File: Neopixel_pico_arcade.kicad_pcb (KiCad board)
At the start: 4 copper layers, 100 x 100 mm, 147 parts, among them J1 SWD_connector, J2 NES_controller_connector, J3 USB_C_Receptacle_USB2.0, Q1 2N7002, U1 RP2040_Stamp, U2 SN74LV1T34DBV, U3 SRV05-4HTG-D

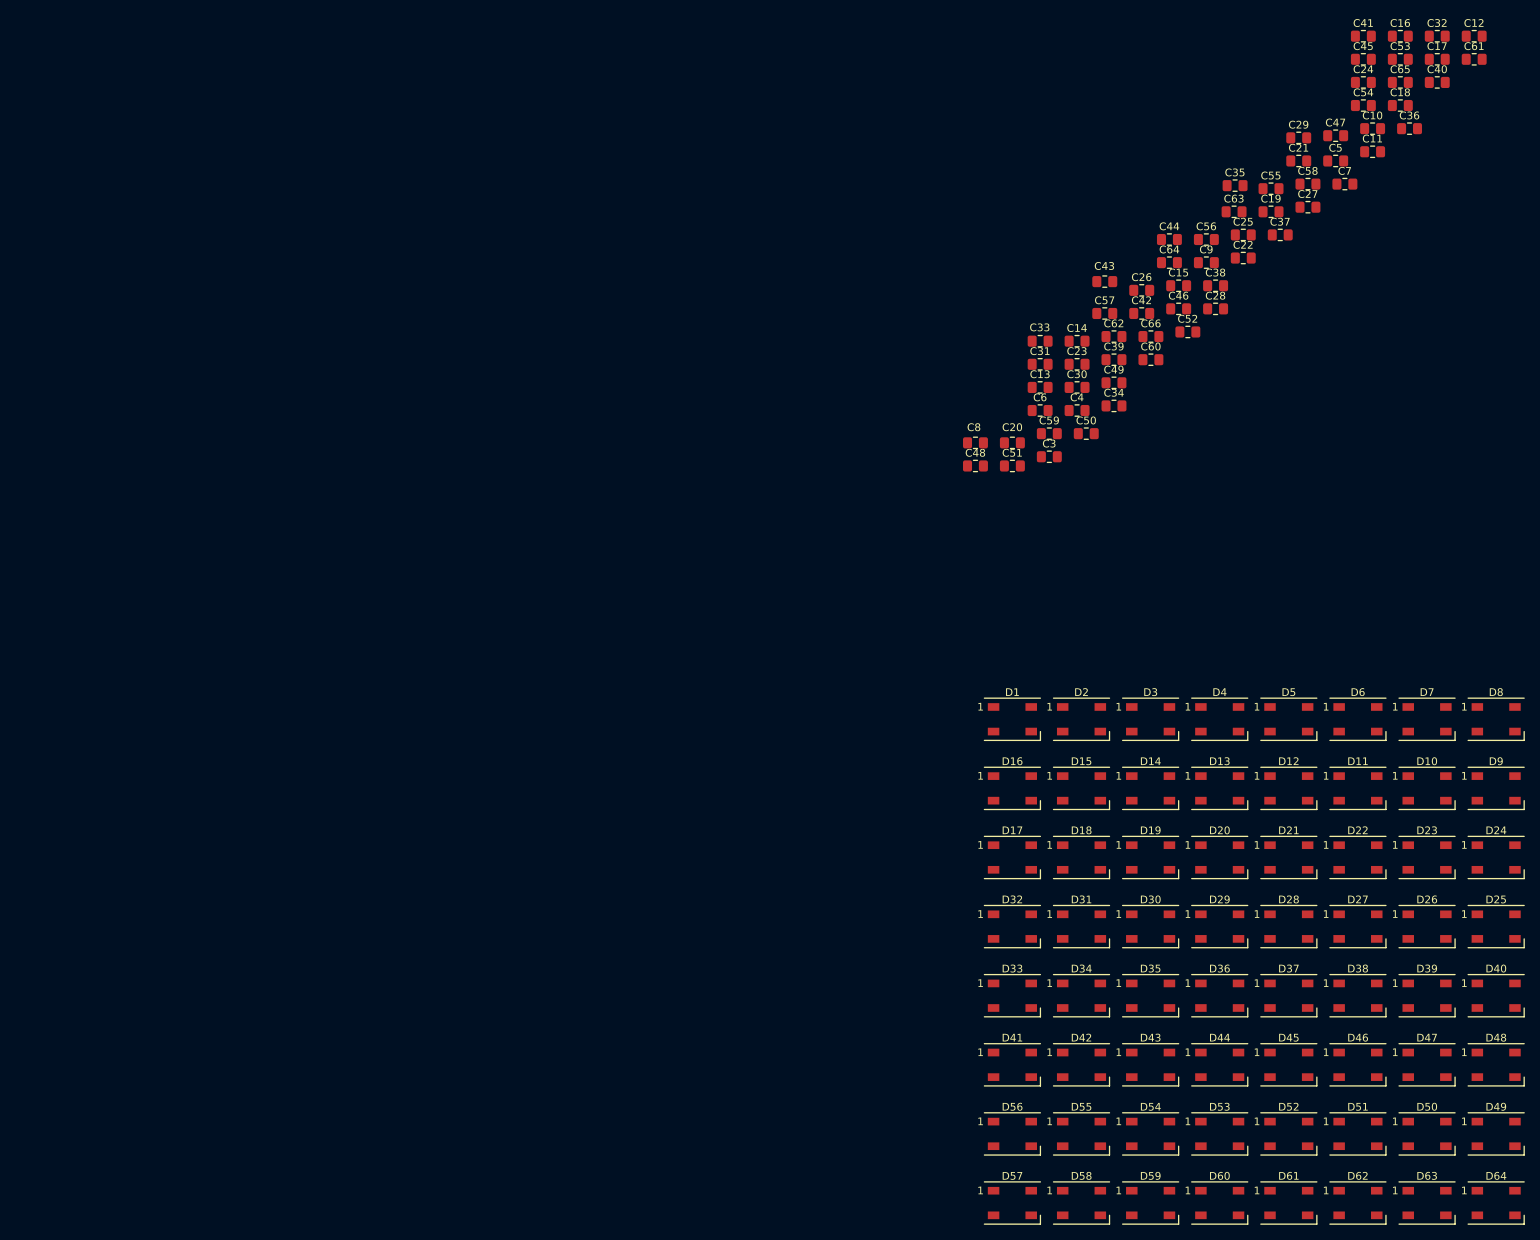
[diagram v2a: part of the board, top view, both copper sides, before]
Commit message: Arranges capacitors in the LED matrix
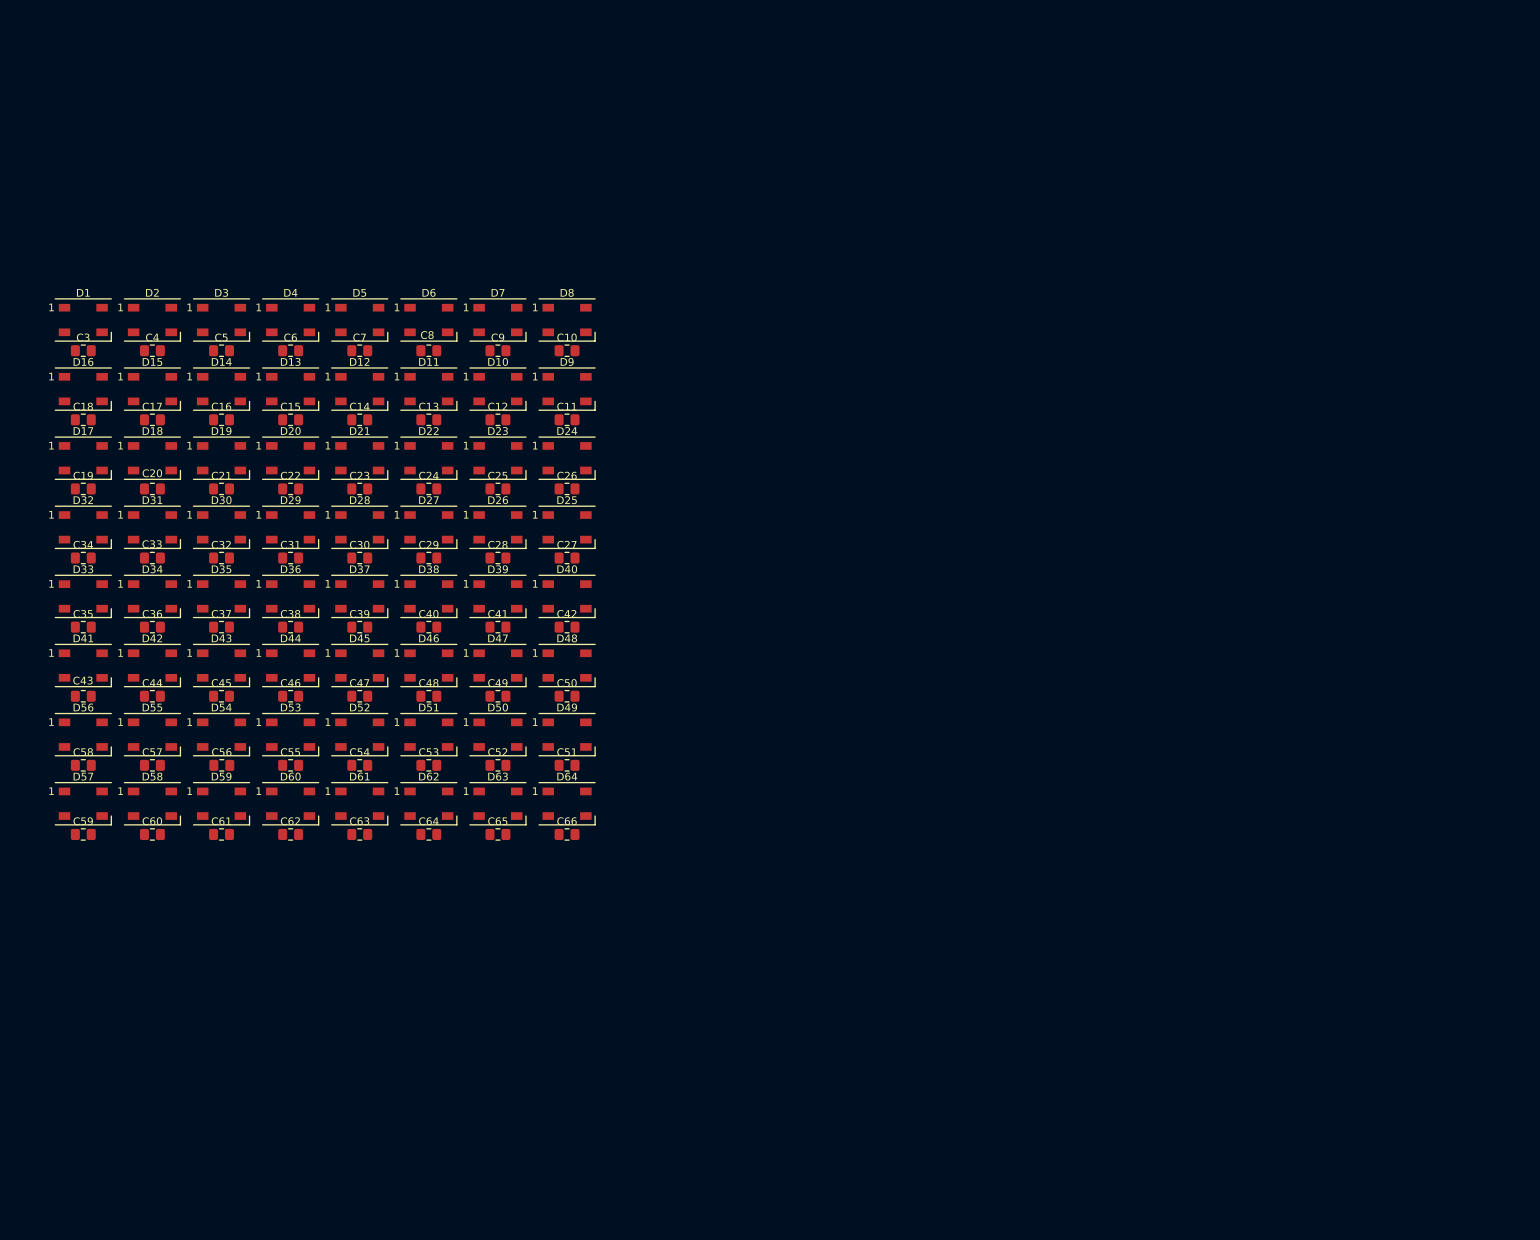
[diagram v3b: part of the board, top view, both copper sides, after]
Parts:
- moved C61 191.8 mm to (240.0, 135.0)
- moved C58 176.5 mm to (222.0, 126.0)
- moved C18 176.3 mm to (222.0, 81.0)
- moved C36 176.1 mm to (231.0, 108.0)
- moved C17 173.8 mm to (231.0, 81.0)
- moved C32 172.3 mm to (240.0, 99.0)
- moved C45 170.3 mm to (240.0, 117.0)
- moved C16 161.4 mm to (240.0, 81.0)
- moved C35 160.6 mm to (222.0, 108.0)
- moved C19 158.8 mm to (222.0, 90.0)
- moved C54 156.4 mm to (258.0, 126.0)
- moved C53 156.4 mm to (267.0, 126.0)
- moved C65 153.0 mm to (276.0, 135.0)
- moved C40 149.3 mm to (267.0, 108.0)
- moved C55 148.1 mm to (249.0, 126.0)
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
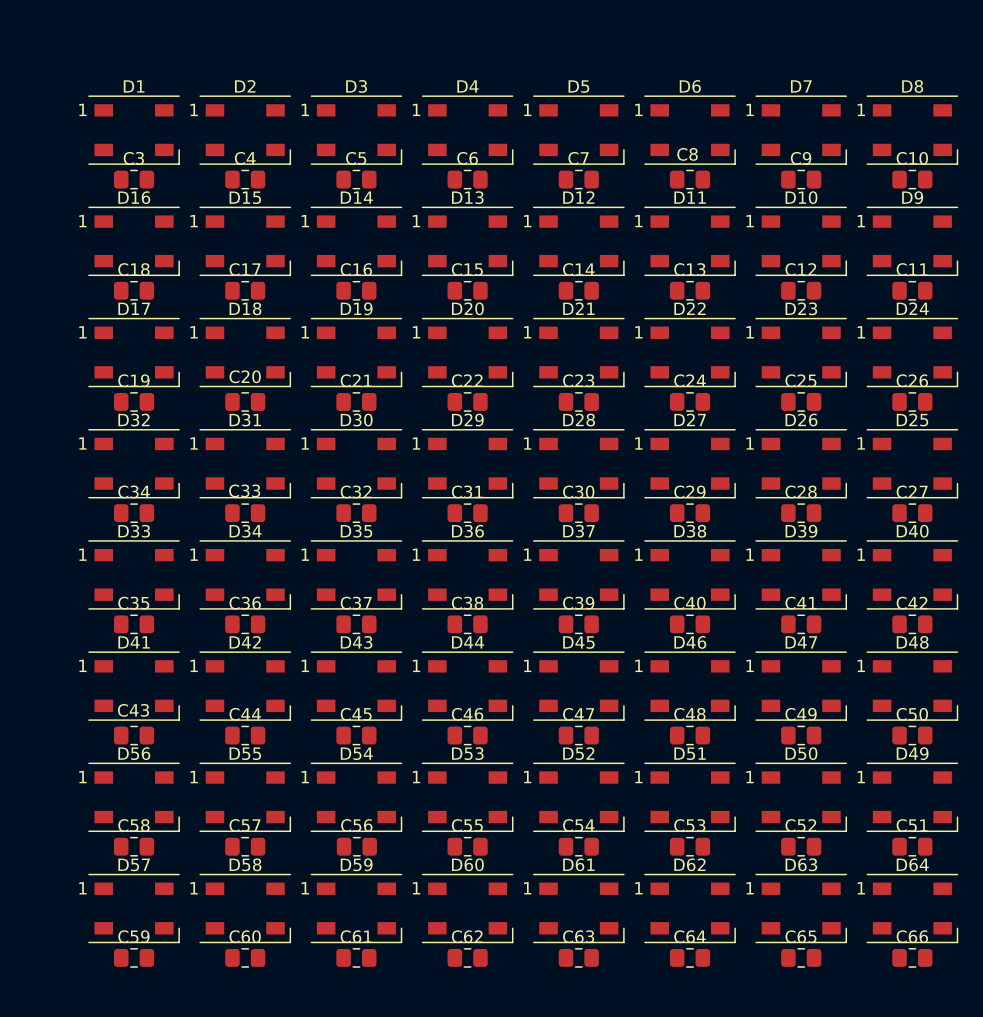
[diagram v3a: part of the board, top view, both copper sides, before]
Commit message: Uses a copy of the built-in WS2812B footprint but with hidden silkscreen
Since this will be the screen, it's better to have no visible silkscreen.
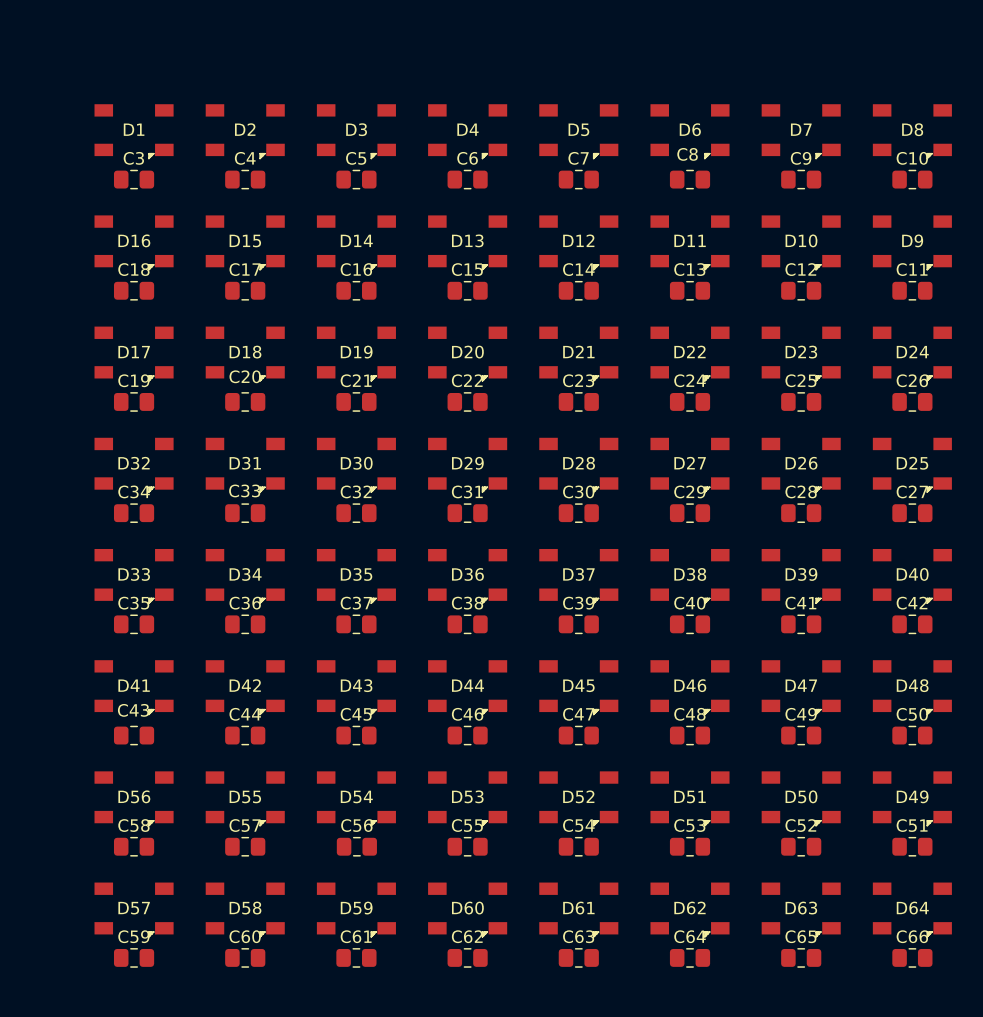
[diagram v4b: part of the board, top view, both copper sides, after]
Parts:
- D1, D10, D11, D12, D13, D14, D15, D16, D17, D18, D19, D2, D20, D21, D22, D23, D24, D25, D26, D27, D28, D29, D3, D30, D31, D32, D33, D34, D35, D36, D37, D38, D39, D4, D40, D41, D42, D43, D44, D45, D46, D47, D48, D49, D5, D50, D51, D52, D53, D54, D55, D56, D57, D58, D59, D6, D60, D61, D62, D63, D64, D7, D8, D9: footprint LED_SMD:LED_WS2812B_PLCC4_5.0x5.0mm_P3.2mm -> Neopixel_pico_arcade:LED_WS2812C_HIDDEN_SILKSCREEN_5.0x5.0mm_P3.2mm

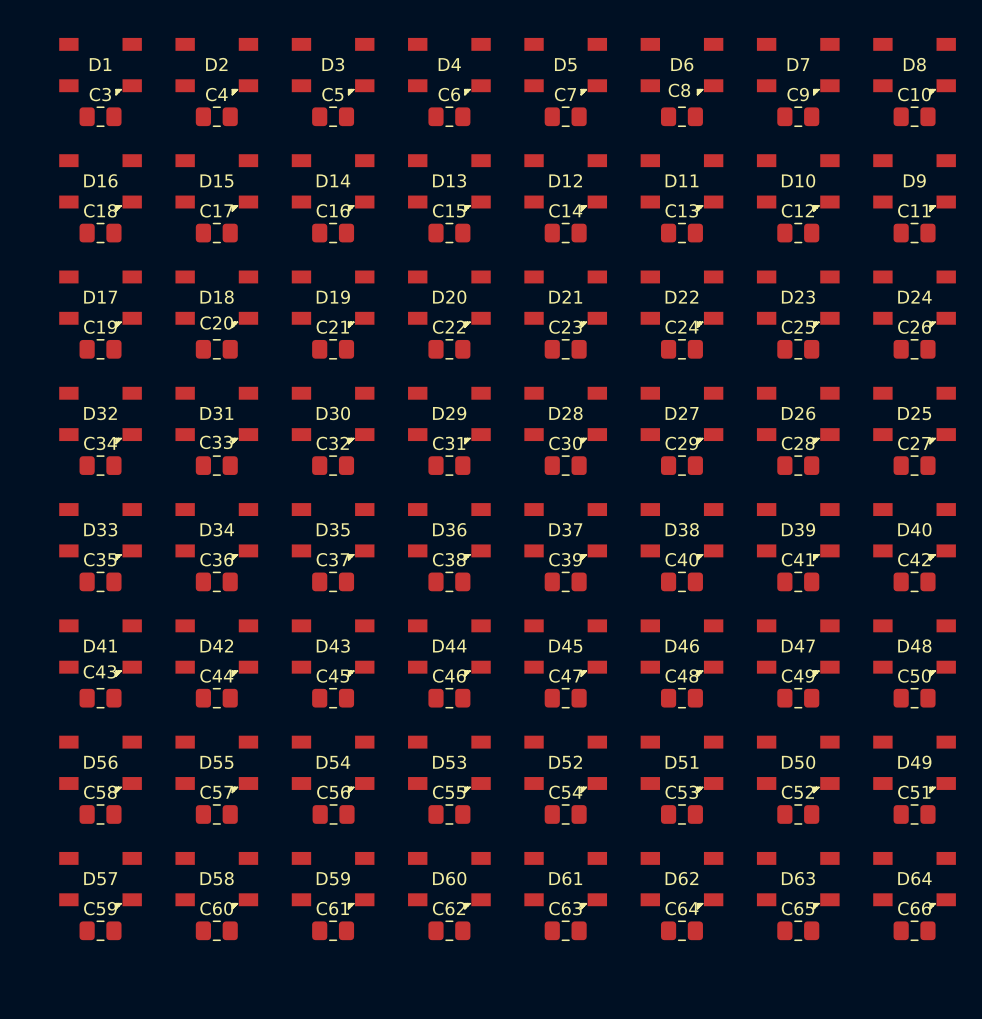
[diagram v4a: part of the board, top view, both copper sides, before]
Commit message: Adds a copy of the built-in 0805 capacitor footprint with no silkscreen
For the same reason we hid the LED silkscreen.
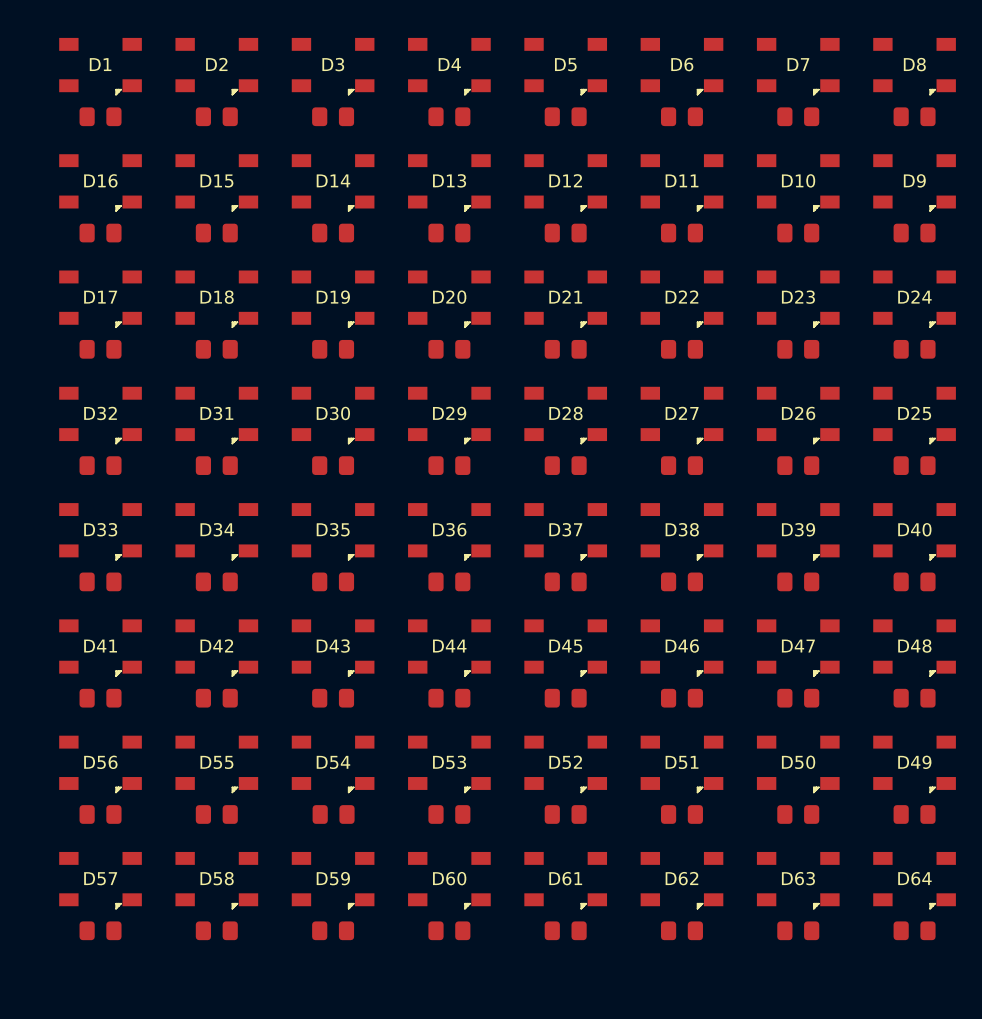
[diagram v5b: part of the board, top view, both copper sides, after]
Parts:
- C10, C11, C12, C13, C14, C15, C16, C17, C18, C19, C20, C21, C22, C23, C24, C25, C26, C27, C28, C29, C3, C30, C31, C32, C33, C34, C35, C36, C37, C38, C39, C4, C40, C41, C42, C43, C44, C45, C46, C47, C48, C49, C5, C50, C51, C52, C53, C54, C55, C56, C57, C58, C59, C6, C60, C61, C62, C63, C64, C65, C66, C7, C8, C9: footprint Capacitor_SMD:C_0805_2012Metric_Pad1.18x1.45mm_HandSolder -> Neopixel_pico_arcade:C_0805_hidden_silkscreen_2012Metric_Pad1.18x1.45mm_HandSolder
